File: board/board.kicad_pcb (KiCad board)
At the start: 2 copper layers, 146.3 x 61.2 mm, 20 parts, among them J1 FTDI_ISP, J2 ICSP, J3 Motor_Terminal, J4 Power, SW1 Run, SW2 Select, SW3 Up, SW4 Down, U1 ATmega328P-P, U2 TSR_1-2450e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

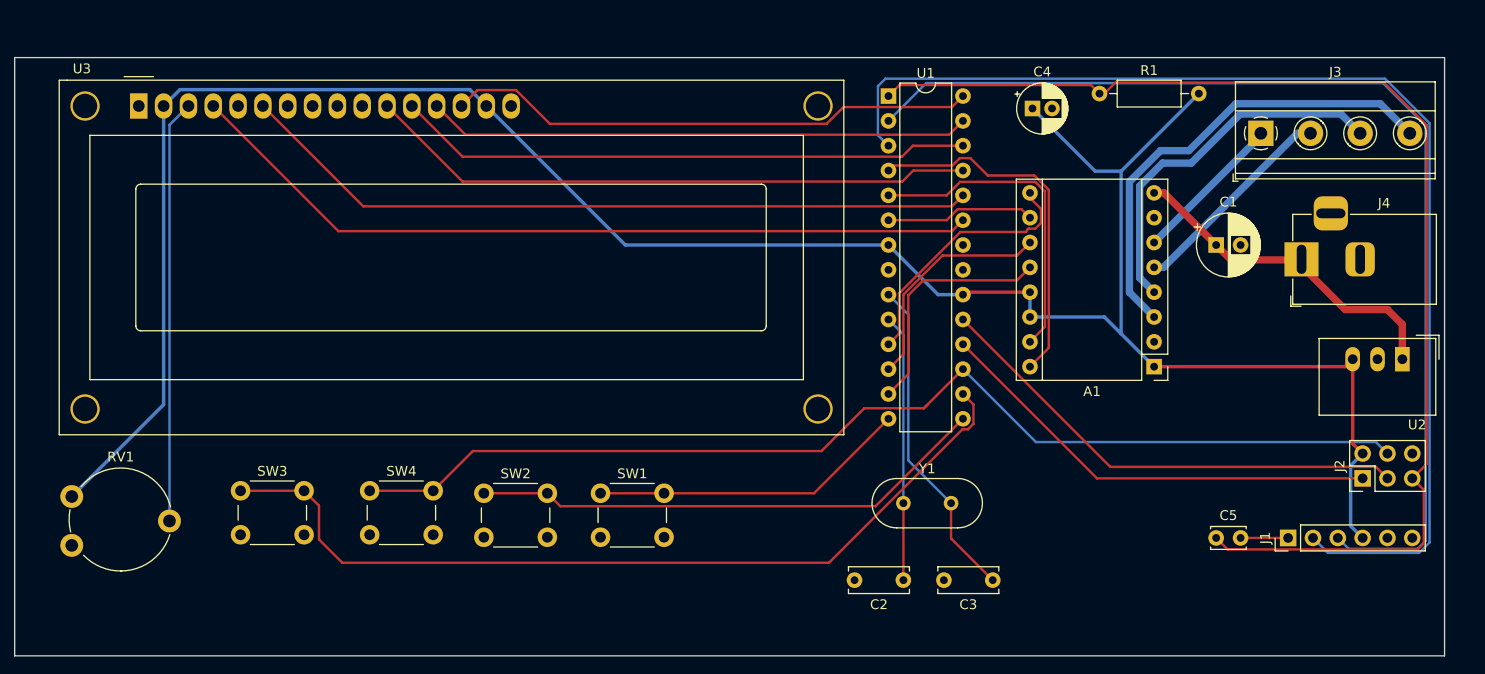
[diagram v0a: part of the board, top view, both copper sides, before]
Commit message: Updted PCB for new SSD1306 display.
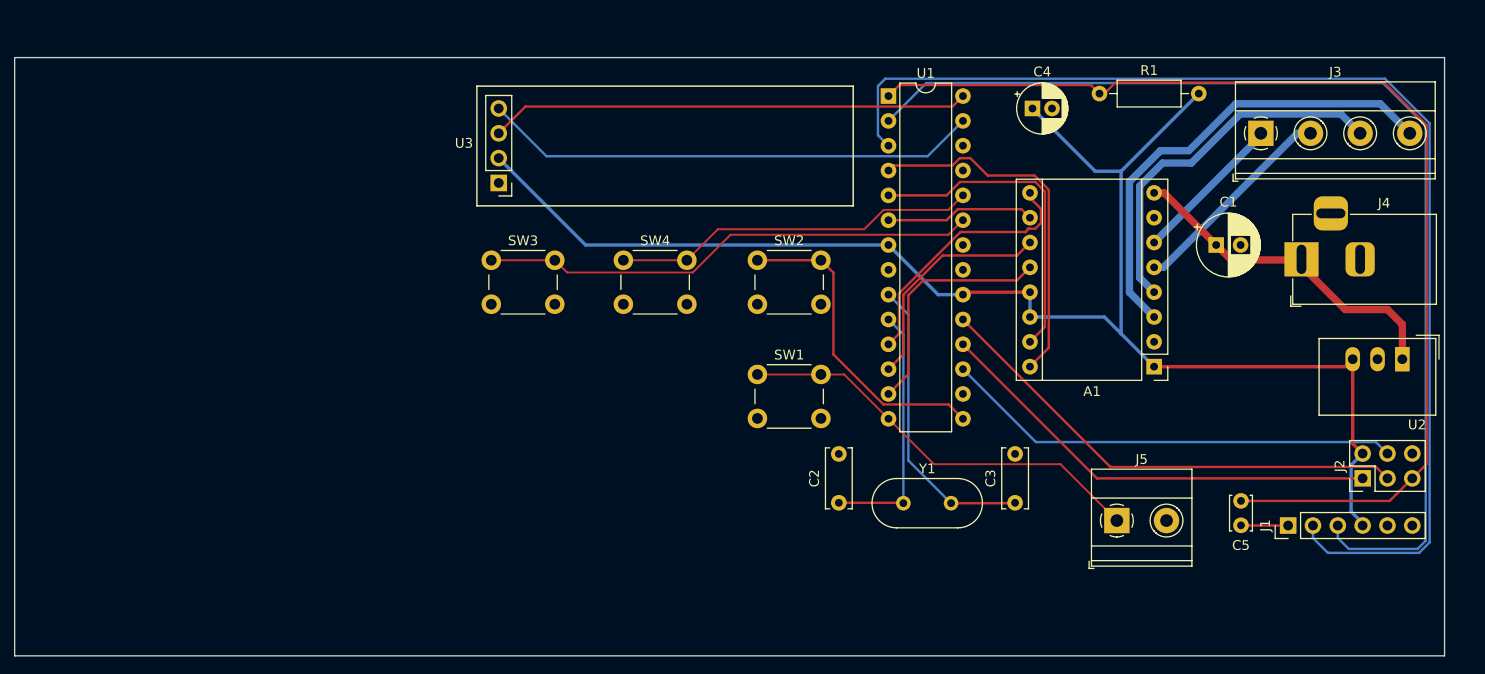
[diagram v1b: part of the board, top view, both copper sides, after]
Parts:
- removed RV1: 10k, Potentiometer_THT:Potentiometer_Piher_PT-10-V10_Vertical
- added J5: Run, TerminalBlock_Phoenix:TerminalBlock_Phoenix_MKDS-1,5-2-5.08_1x02_P5.08mm_Horizontal, F.Cu at (196.8, 78.5)
- U3: value NHD-0216K1Z -> SSD1306; footprint Display:WC1602A -> Connector_PinHeader_2.54mm:PinHeader_1x04_P2.54mm_Vertical
- moved U3 37.7 mm to (133.6, 43.9), turned to 180 degrees
- moved SW2 36.8 mm to (160.1, 51.9)
- moved SW4 35.1 mm to (146.4, 51.9)
- moved SW3 34.8 mm to (132.8, 51.9)
- moved SW1 20.1 mm to (160.1, 63.5)
- moved C2 10.3 mm to (168.4, 76.7), turned to 90 degrees
- moved C3 8.24 mm to (186.4, 76.7), turned to 90 degrees
- moved C5 4.56 mm to (209.6, 76.5), turned to -90 degrees
- moved J1 1.27 mm to (214.4, 79.0)
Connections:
- J2 pad 4: MOSI_BTN_DOWN -> MOSI
- SW4 pad 1: MOSI_BTN_DOWN -> BTN_DOWN
- U1 pad 16: BTN_UP -> unconnected-(U1-Pad16)
- U1 pad 17: MOSI_BTN_DOWN -> MOSI
- U1 pad 23: LCD_RS -> BTN_UP
- U1 pad 24: LCD_E -> BTN_DOWN
- U1 pad 25: LCD_D4 -> unconnected-(U1-Pad25)
- U1 pad 26: LCD_D5 -> unconnected-(U1-Pad26)
- U1 pad 27: LCD_D6 -> SDA
- U1 pad 28: LCD_D7 -> SCL
- U3 pad 3: Net-(RV1-Pad2) -> SCL
- U3 pad 4: LCD_RS -> SDA
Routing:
- net MOSI_BTN_DOWN: track 113.4 -> 0.00 mm
- net +5V: track 239.6 -> 156.6 mm
- net LCD_RS: track 82.5 -> 0.00 mm
- net LCD_E: track 76.3 -> 0.00 mm
- net LCD_D4: track 62.6 -> 0.00 mm
- net LCD_D5: track 59.0 -> 0.00 mm
- net LCD_D6: track 55.7 -> 0.00 mm
- net LCD_D7: track 54.6 -> 0.00 mm
- net SDA: track 0.00 -> 51.0 mm
- net SCL: track 0.00 -> 49.1 mm
- net MOSI: track 0.00 -> 47.0 mm
- net Net-(RV1-Pad2): track 43.3 -> 0.00 mm
- net BTN_UP: track 89.5 -> 51.0 mm
- net BTN_DOWN: track 0.00 -> 37.5 mm
- net BTN_SEL: track 53.3 -> 32.6 mm
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
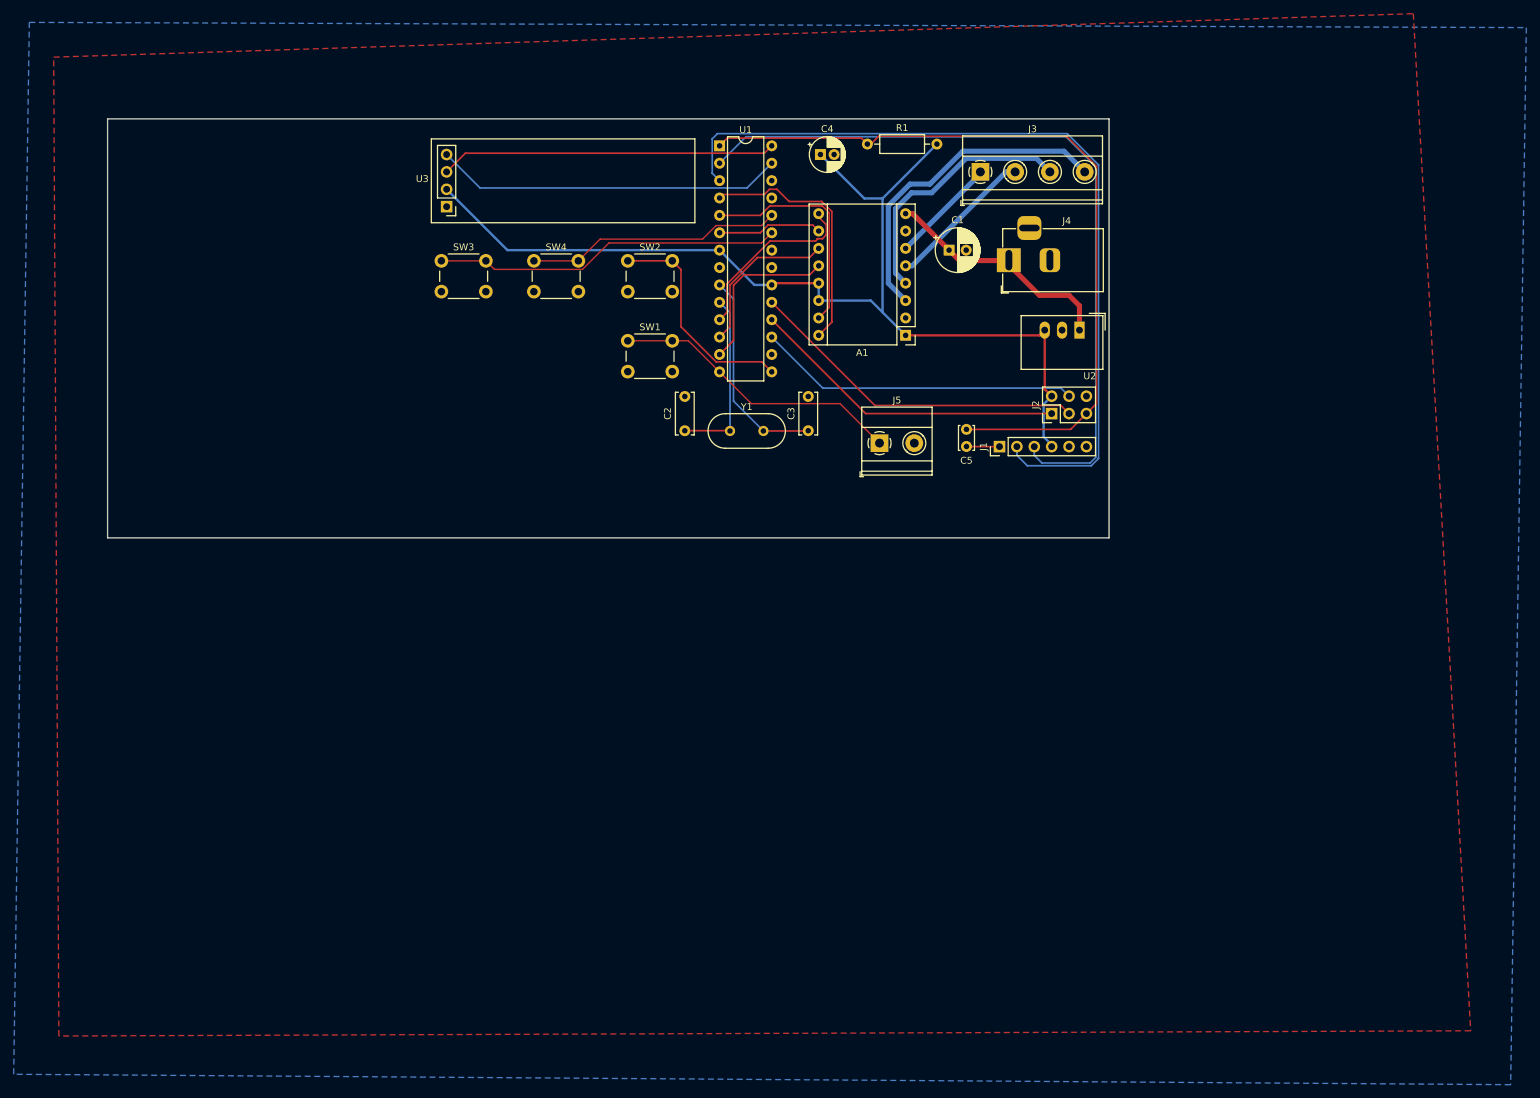
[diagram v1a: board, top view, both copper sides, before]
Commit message: Update parts, enable drill files.
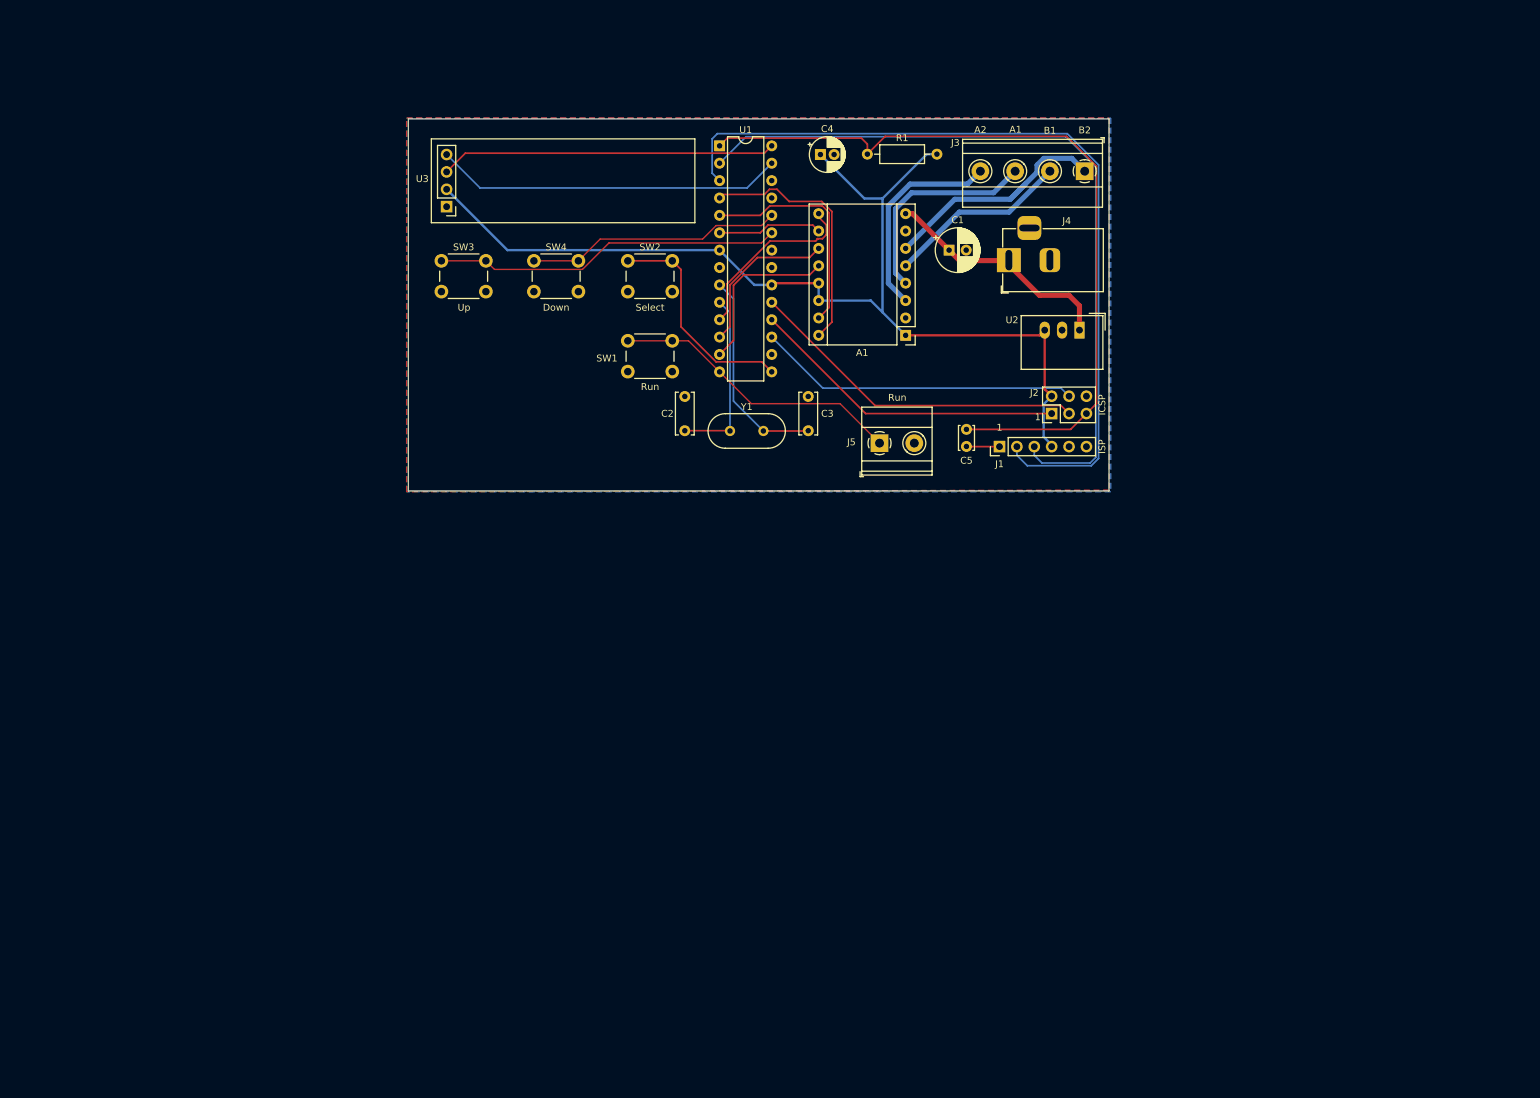
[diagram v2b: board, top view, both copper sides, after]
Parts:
- moved J3 15.2 mm to (226.8, 38.8), turned to 180 degrees
- moved R1 1.47 mm to (195.1, 36.3)
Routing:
- net MOT_B2: track 16.0 -> 36.4 mm
- net MOT_A2: track 48.1 -> 30.7 mm
- net MOT_A1: track 37.9 -> 31.2 mm
- net MOT_B1: track 22.0 -> 27.1 mm
- net RESET: track 113.4 -> 115.5 mm
- net +5V: track 156.6 -> 156.0 mm
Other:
- board size 146.3 x 61.2 mm -> 102.4 x 54.4 mm
- board text added: "1"
- board text added: "A1"
- board text added: "A2"
- board text added: "B1"
- board text added: "B2"
- board text added: "Down"
- board text added: "ICSP"
- board text added: "ISP"
- board text added: "Run"
- board text added: "Select"
- board text added: "Up"
